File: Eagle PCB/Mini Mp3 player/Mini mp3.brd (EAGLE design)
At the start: 115.5 x 58.1 mm, 16 parts, among them U2 ATMEGA328P-PU

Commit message: updated board
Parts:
- moved SPK2 8.98 mm to (102.9, 2.54)
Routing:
- net N$1: track 164.0 -> 66.8 mm
- net 5.5V: track 160.2 -> 238.4 mm
- net N$12: track 58.3 -> 134.9 mm
- net N$2: track 158.2 -> 83.1 mm
- net 0: track 408.6 -> 372.1 mm
- net N$5: track 58.7 -> 28.6 mm
- net S: track 64.2 -> 48.9 mm
- net N$3: track 78.3 -> 68.3 mm
- net N$10: track 72.9 -> 64.6 mm
- net N$11: track 66.1 -> 73.4 mm
- net N$6: track 36.7 -> 43.0 mm
- net N$16: track 75.7 -> 81.5 mm
- net N$14: track 73.3 -> 71.9 mm
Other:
- board text added: "EZ Clap - Gex"

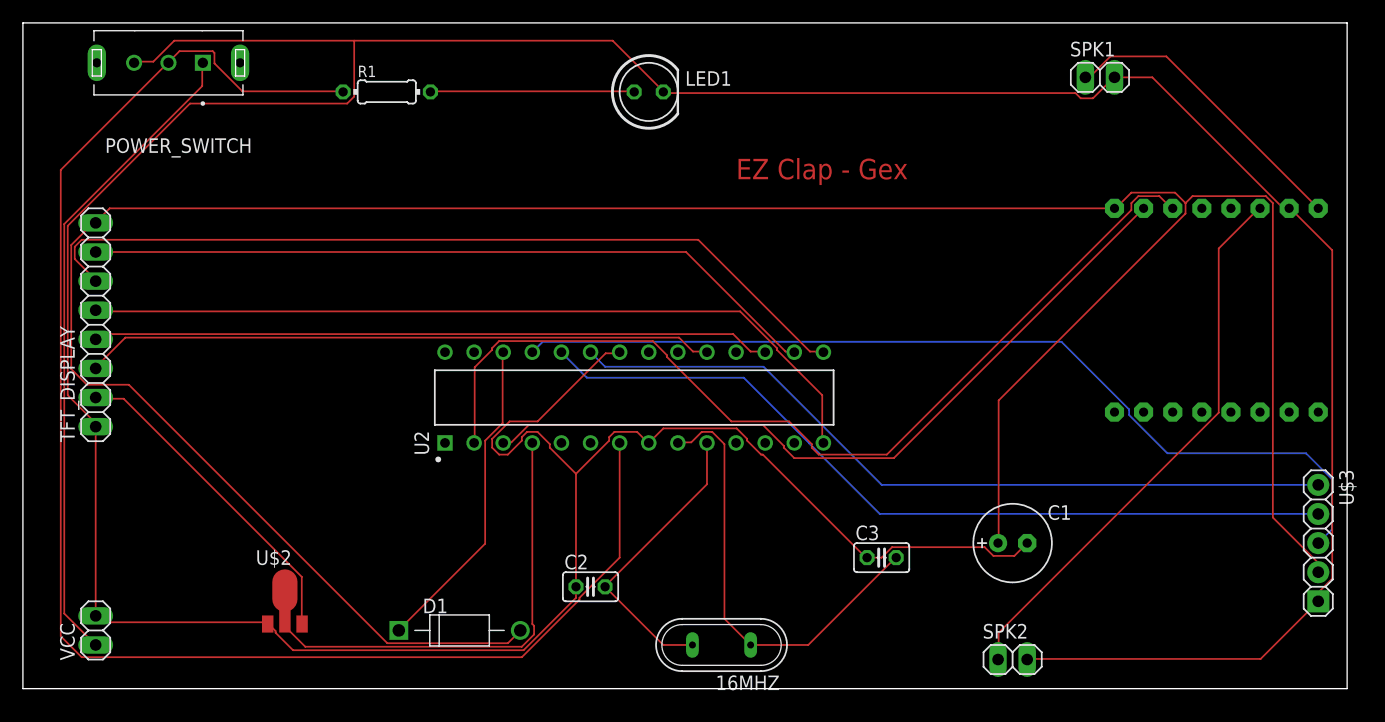
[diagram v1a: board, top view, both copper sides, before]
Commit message: Voltage divider included and updated Mini display
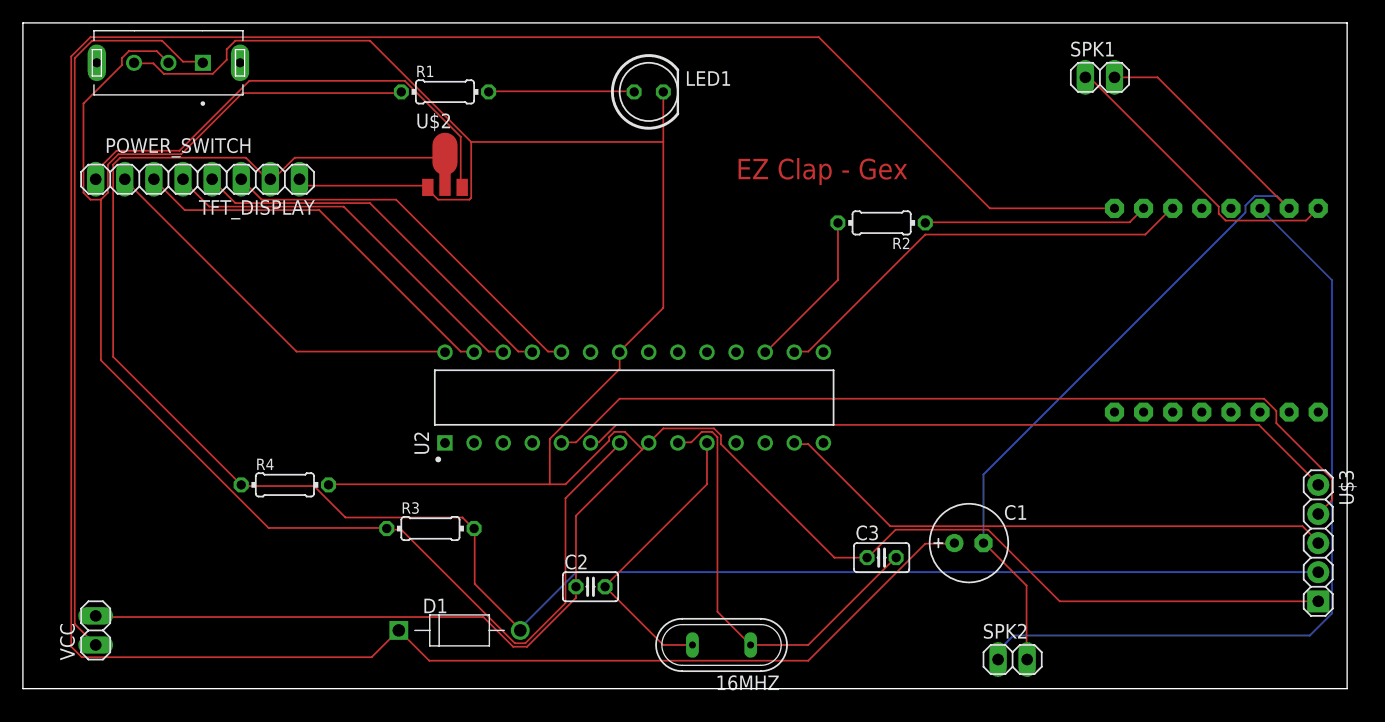
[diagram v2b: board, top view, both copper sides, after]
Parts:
- added R2: 1K, rcl:0204/7
- added R3: 6.8K, rcl:0204/7
- added R4: 10k, rcl:0204/7
- moved U$2 40.6 mm to (53.3, 45.7)
- moved TFT_DISPLAY 15.5 mm to (31.8, 44.5), turned to 180 degrees
- moved R1 5.08 mm to (53.3, 52.1)
- moved C1 3.81 mm to (99.1, 12.7)
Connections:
- removed net 5.5V: C1.+, D1.A, TFT_DISPLAY.8, U$1.VCC, U$3.VCC
- new net +5V: D1.A, R3.2, R4.1, TFT_DISPLAY.2, U$2.2, U$2.2@1, U$3.VCC
- new net N$20: U$3.CLK, U2.6
- net 0: now also R4.2; no longer C1.-, SPK1.2, SPK2.2, U$1.GND_1
- net N$1: now also R2.2, U2.17; no longer U$1.RX, U2.3
- net N$10: now also C1.-, SPK1.2, SPK2.2, U$1.GND_1; no longer TFT_DISPLAY.7, U2.16
- net N$11: now also C1.+, D1.C, U$1.VCC; no longer TFT_DISPLAY.6, U2.15
- net N$12: now also R3.1
- net N$14: now also R2.1, U$1.RX; no longer U$3.DT, U2.24
- net N$15: now also U$3.SW, U2.13; no longer D1.C, U2.26
- net N$16: now also U$3.DT, U2.5; no longer U$3.SW, U2.25
- net N$2: now also U2.16; no longer U2.2
- net N$3: now also TFT_DISPLAY.6, U2.27; no longer U$3.CLK, U2.23
- net N$5: now also TFT_DISPLAY.8; no longer TFT_DISPLAY.2
- net N$6: now also TFT_DISPLAY.7, U2.28; no longer U$2.2, U$2.2@1, U2.4
- net N$7: now also TFT_DISPLAY.5, U2.26; no longer TFT_DISPLAY.3, U2.19
- net N$8: now also U2.25; no longer U2.17
- net N$9: now also TFT_DISPLAY.3, U2.24; no longer TFT_DISPLAY.5, U2.14
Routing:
- net 5.5V: track 238.4 -> 0.00 mm
- net +5V: track 0.00 -> 170.3 mm
- net N$11: track 73.4 -> 233.2 mm
- net 0: track 372.1 -> 270.0 mm
- net N$20: track 0.00 -> 66.3 mm
- net N$1: track 66.8 -> 13.9 mm
- net N$14: track 71.9 -> 19.6 mm
- net N$2: track 83.1 -> 38.2 mm
- net N$9: track 70.8 -> 34.2 mm
- net N$3: track 68.3 -> 34.2 mm
- net N$8: track 59.3 -> 34.2 mm
- net N$15: track 28.0 -> 49.5 mm
- net N$7: track 55.1 -> 34.3 mm
- net S: track 48.9 -> 69.2 mm
- net N$5: track 28.6 -> 42.3 mm
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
